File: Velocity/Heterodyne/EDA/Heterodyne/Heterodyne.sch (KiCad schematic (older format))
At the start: 40 parts, among them J1 OP_IN, J2 OP_OUT, J3 PWR, J4 Doppler_Out, J5 V_Square, J6 OP_OUT, J7 Reciever, J8 Emmiter, U1 SA612AD, U2 NE5532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

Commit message: changed up velocity heterodyne schematic to fix issues with wireing, and so provide a channel for sine wave driver amplification
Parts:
- removed C3, C4, C5: 100 nF, Capacitors_SMD:C_0805_HandSoldering, symbol Heterodyne-rescue:C-Device
- removed J1: OP_IN, Pin_Headers:Pin_Header_Straight_1x02_Pitch2.54mm, symbol Heterodyne-rescue:Conn_01x02-Connector_Generic
- removed J2: OP_OUT, Pin_Headers:Pin_Header_Straight_1x02_Pitch2.54mm, symbol Heterodyne-rescue:Conn_01x02-Connector_Generic
- removed R1, R3, R4, R5: 10 kΩ, Resistors_SMD:R_0805_HandSoldering, symbol Heterodyne-rescue:R-Device
- added R?: 39 kΩ, Resistors_SMD:R_0805_HandSoldering, symbol Heterodyne-rescue:R-Device
- added R? (x2): 1 kΩ, Resistors_SMD:R_0805_HandSoldering, symbol Heterodyne-rescue:R-Device
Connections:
- net GND: now also U2.4 (V-), R?.1; no longer U2.8 (V+)
- net VPP: now also U2.8 (V+), R?.1; no longer U2.4 (V-)
- net at J6.2 (Pin_2), U2.1: now also R?.2
- net at U2.2 (-): now also R?.1, R?.2, R?.2
- net Driver_Wave: now reaches U2.3 (+)
- net Driver_Wave: now also C10.2, C9.1, R10.2
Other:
- note added: "Consider Changing op amp to TL074"
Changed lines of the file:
@@
 L Heterodyne-rescue:NE5532-Amplifier_Operational U2
 U 3 1 5DE9ED64
-P 8250 3600
-F 0 "U2" H 8063 3555 50  0000 R CNN
-F 1 "NE5532" H 8063 3644 50  0000 R CNN
-F 2 "Housings_DIP:DIP-8_W7.62mm_LongPads" H 8250 3600 50  0001 C CNN
-F 3 "http://www.ti.com/lit/ds/symlink/ne5532.pdf" H 8250 3600 50  0001 C CNN
-	3    8250 3600
-	-1   0    0    1
-$EndComp
-$Comp
-L Heterodyne-rescue:VPP-power #PWR0111
-U 1 1 5DEA1CC4
-P 8350 3300
-F 0 "#PWR0111" H 8350 3150 50  0001 C CNN
-F 1 "VPP" V 8365 3426 50  0000 L CNN
-F 2 "" H 8350 3300 50  0001 C CNN
-F 3 "" H 8350 3300 50  0001 C CNN
-	1    8350 3300
-	1    0    0    -1
-$EndComp
-$Comp
-L Heterodyne-rescue:GND-power #PWR0112
-U 1 1 5DEA21FC
-P 8350 3900
-F 0 "#PWR0112" H 8350 3650 50  0001 C CNN
-F 1 "GND" V 8355 3773 50  0000 R CNN
-F 2 "" H 8350 3900 50  0001 C CNN
-F 3 "" H 8350 3900 50  0001 C CNN
-	1    8350 3900
+P 8450 3600
+F 0 "U2" H 8263 3555 50  0000 R CNN
+F 1 "NE5532" H 8263 3644 50  0000 R CNN
+F 2 "Housings_DIP:DIP-8_W7.62mm_LongPads" H 8450 3600 50  0001 C CNN
+F 3 "http://www.ti.com/lit/ds/symlink/ne5532.pdf" H 8450 3600 50  0001 C CNN
+	3    8450 3600
 	1    0    0    -1
 $EndComp
@@
 	0    -1   1    0
 $EndComp
-$Comp
-L Heterodyne-rescue:GND-power #PWR0117
-U 1 1 5DEC862E
-P 2450 2400
-F 0 "#PWR0117" H 2450 2150 50  0001 C CNN
-F 1 "GND" V 2455 2273 50  0000 R CNN
-F 2 "" H 2450 2400 50  0001 C CNN
-F 3 "" H 2450 2400 50  0001 C CNN
-	1    2450 2400
-	1    0    0    -1
-$EndComp
-$Comp
-L Heterodyne-rescue:GND-power #PWR0118
-U 1 1 5DEC895C
-P 1950 2400
-F 0 "#PWR0118" H 1950 2150 50  0001 C CNN
-F 1 "GND" V 1955 2273 50  0000 R CNN
-F 2 "" H 1950 2400 50  0001 C CNN
-F 3 "" H 1950 2400 50  0001 C CNN
-	1    1950 2400
-	1    0    0    -1
-$EndComp
-$Comp
-L Heterodyne-rescue:Conn_01x02-Connector_Generic J1
-U 1 1 5DECC74B
-P 2350 2200
-F 0 "J1" H 2430 2192 50  0000 L CNN
-F 1 "OP_IN" H 2430 2103 50  0000 L CNN
-F 2 "Pin_Headers:Pin_Header_Straight_1x02_Pitch2.54mm" H 2350 2200 50  0001 C CNN
-F 3 "~" H 2350 2200 50  0001 C CNN
-	1    2350 2200
-	0    -1   -1   0
-$EndComp
-$Comp
-L Heterodyne-rescue:Conn_01x02-Connector_Generic J2
-U 1 1 5DECCC45
-P 1950 2200
-F 0 "J2" H 2030 2192 50  0000 L CNN
-F 1 "OP_OUT" H 2030 2103 50  0000 L CNN
-F 2 "Pin_Headers:Pin_Header_Straight_1x02_Pitch2.54mm" H 1950 2200 50  0001 C CNN
-F 3 "~" H 1950 2200 50  0001 C CNN
-	1    1950 2200
-	0    -1   -1   0
-$EndComp
 Connection ~ 6150 4050
 Wire Wire Line
@@
 	5250 5100 5650 5100
 $Comp
-L Heterodyne-rescue:R-Device R4
-U 1 1 5DFAD002
-P 2350 2900
-F 0 "R4" V 2554 2900 50  0000 C CNN
-F 1 "10 kΩ" V 2465 2900 50  0000 C CNN
-F 2 "Resistors_SMD:R_0805_HandSoldering" V 2280 2900 50  0001 C CNN
-F 3 "~" H 2350 2900 50  0001 C CNN
-	1    2350 2900
-	1    0    0    -1
-$EndComp
-$Comp
-L Heterodyne-rescue:R-Device R3
-U 1 1 5DFAD398
-P 2050 2900
-F 0 "R3" V 2254 2900 50  0000 C CNN
-F 1 "10 kΩ" V 2165 2900 50  0000 C CNN
-F 2 "Resistors_SMD:R_0805_HandSoldering" V 1980 2900 50  0001 C CNN
-F 3 "~" H 2050 2900 50  0001 C CNN
-	1    2050 2900
-	1    0    0    -1
-$EndComp
-$Comp
-L Heterodyne-rescue:C-Device C4
-U 1 1 5DFADDA3
-P 2200 3250
-F 0 "C4" H 2085 3205 50  0000 R CNN
-F 1 "100 nF" H 2085 3294 50  0000 R CNN
-F 2 "Capacitors_SMD:C_0805_HandSoldering" H 2238 3100 50  0001 C CNN
-F 3 "~" H 2200 3250 50  0001 C CNN
-	1    2200 3250
-	0    -1   -1   0
-$EndComp
-$Comp
-L Heterodyne-rescue:R-Device R5
-U 1 1 5DFAEA80
-P 2600 3850
-F 0 "R5" V 2804 3850 50  0000 C CNN
-F 1 "10 kΩ" V 2715 3850 50  0000 C CNN
-F 2 "Resistors_SMD:R_0805_HandSoldering" V 2530 3850 50  0001 C CNN
-F 3 "~" H 2600 3850 50  0001 C CNN
-	1    2600 3850
-	1    0    0    -1
-$EndComp
-$Comp
-L Heterodyne-rescue:R-Device R1
-U 1 1 5DFAEDEA
-P 1450 3850
-F 0 "R1" V 1654 3850 50  0000 C CNN
-F 1 "10 kΩ" V 1565 3850 50  0000 C CNN
-F 2 "Resistors_SMD:R_0805_HandSoldering" V 1380 3850 50  0001 C CNN
-F 3 "~" H 1450 3850 50  0001 C CNN
-	1    1450 3850
-	1    0    0    -1
-$EndComp
-$Comp
-L Heterodyne-rescue:C-Device C5
-U 1 1 5DFAF0E1
-P 2950 3850
-F 0 "C5" V 3199 3850 50  0000 C CNN
-F 1 "100 nF" V 3110 3850 50  0000 C CNN
-F 2 "Capacitors_SMD:C_0805_HandSoldering" H 2988 3700 50  0001 C CNN
-F 3 "~" H 2950 3850 50  0001 C CNN
-	1    2950 3850
-	1    0    0    -1
-$EndComp
-$Comp
-L Heterodyne-rescue:C-Device C3
-U 1 1 5DFB2EFF
-P 1100 3850
-F 0 "C3" V 1349 3850 50  0000 C CNN
-F 1 "100 nF" V 1260 3850 50  0000 C CNN
-F 2 "Capacitors_SMD:C_0805_HandSoldering" H 1138 3700 50  0001 C CNN
-F 3 "~" H 1100 3850 50  0001 C CNN
-	1    1100 3850
-	1    0    0    -1
-$EndComp
-$Comp
 L Heterodyne-rescue:GND-power #PWR0120
 U 1 1 5DFB3A2A
@@
 $EndComp
 Wire Wire Line
-	2150 4150 2600 4150
-Wire Wire Line
-	2600 4150 2600 4000
-Wire Wire Line
-	2350 3050 2350 3250
-Wire Wire Line
-	2350 3250 2350 3550
-Wire Wire Line
 	2250 3550 2350 3550
-Connection ~ 2350 3250
 Connection ~ 2350 3550
-Wire Wire Line
-	2350 3550 2600 3550
-Wire Wire Line
-	2050 3550 2050 3250
-Wire Wire Line
-	2050 3250 2050 3050
-Connection ~ 2050 3250
-Wire Wire Line
-	2350 2400 2350 2750
-Wire Wire Line
-	2050 2400 2050 2750
-Wire Wire Line
-	2950 4000 2950 4150
-Wire Wire Line
-	2950 4150 2600 4150
-Connection ~ 2600 4150
-Wire Wire Line
-	2950 3700 2950 3550
-Wire Wire Line
-	2950 3550 2600 3550
-Connection ~ 2600 3550
-Wire Wire Line
-	2050 3250 1450 3250
-Wire Wire Line
-	1450 3250 1450 3700
-Wire Wire Line
-	1450 3250 1100 3250
-Wire Wire Line
-	1100 3250 1100 3700
-Wire Wire Line
-	2600 3550 2600 3700
-Connection ~ 1450 3250
-Wire Wire Line
-	1100 4000 1450 4000
-Wire Wire Line
-	2150 4150 1450 4150
-Wire Wire Line
-	1450 4150 1450 4000
-Connection ~ 2150 4150
-Connection ~ 1450 4000
 Wire Wire Line
 	2150 4150 2150 4350
@@
 $EndComp
 Wire Wire Line
-	8350 3300 8050 3300
-Wire Wire Line
 	8050 3300 8050 3450
-Connection ~ 8350 3300
 Wire Wire Line
 	8050 3750 8050 3900
-Wire Wire Line
-	8050 3900 8350 3900
-Connection ~ 8350 3900
 Connection ~ 6900 1850
 Connection ~ 6900 1550
+Wire Wire Line
+	8050 3300 8350 3300
+Wire Wire Line
+	8050 3900 8350 3900
+$Comp
+L Heterodyne-rescue:VPP-power #PWR?
+U 1 1 5E281BA1
+P 8350 3300
+F 0 "#PWR?" H 8350 3150 50  0001 C CNN
+F 1 "VPP" H 8365 3471 50  0000 C CNN
+F 2 "" H 8350 3300 50  0001 C CNN
+F 3 "" H 8350 3300 50  0001 C CNN
+	1    8350 3300
+	1    0    0    -1
+$EndComp
+Connection ~ 8350 3300
+$Comp
+L Heterodyne-rescue:GND-power #PWR?
+U 1 1 5E282178
+P 8350 3900
+F 0 "#PWR?" H 8350 3650 50  0001 C CNN
+F 1 "GND" H 8355 3729 50  0000 C CNN
+F 2 "" H 8350 3900 50  0001 C CNN
+F 3 "" H 8350 3900 50  0001 C CNN
+	1    8350 3900
+	1    0    0    -1
+$EndComp
+Connection ~ 8350 3900
+Wire Wire Line
+	2050 3050 2050 3550
+$Comp
+L Heterodyne-rescue:R-Device R?
+U 1 1 5E282544
+P 2650 3850
+F 0 "R?" V 2854 3850 50  0000 C CNN
+F 1 "39 kΩ" V 2765 3850 50  0000 C CNN
+F 2 "Resistors_SMD:R_0805_HandSoldering" V 2580 3850 50  0001 C CNN
+F 3 "~" H 2650 3850 50  0001 C CNN
+	1    2650 3850
+	1    0    0    -1
+$EndComp
+Wire Wire Line
+	2150 4150 2650 4150
+Wire Wire Line
+	2650 4150 2650 4000
+Connection ~ 2150 4150
+Wire Wire Line
+	2650 3700 2650 3550
+Wire Wire Line
+	2350 3550 2650 3550
+$Comp
+L Heterodyne-rescue:R-Device R?
+U 1 1 5E285F20
+P 2350 2800
+F 0 "R?" V 2554 2800 50  0000 C CNN
+F 1 "1 kΩ" V 2465 2800 50  0000 C CNN
+F 2 "Resistors_SMD:R_0805_HandSoldering" V 2280 2800 50  0001 C CNN
+F 3 "~" H 2350 2800 50  0001 C CNN
+	1    2350 2800
+	1    0    0    -1
+$EndComp
+$Comp
+L Heterodyne-rescue:R-Device R?
+U 1 1 5E286294
+P 2600 3050
+F 0 "R?" V 2804 3050 50  0000 C CNN
+F 1 "1 kΩ" V 2715 3050 50  0000 C CNN
+F 2 "Resistors_SMD:R_0805_HandSoldering" V 2530 3050 50  0001 C CNN
+F 3 "~" H 2600 3050 50  0001 C CNN
+	1    2600 3050
+	0    1    1    0
+$EndComp
+Wire Wire Line
+	2350 2950 2350 3050
+Wire Wire Line
+	2450 3050 2350 3050
+Connection ~ 2350 3050
+Wire Wire Line
+	2350 3050 2350 3550
+$Comp
+L Heterodyne-rescue:VPP-power #PWR?
+U 1 1 5E289D11
+P 2350 2650
+F 0 "#PWR?" H 2350 2500 50  0001 C CNN
+F 1 "VPP" H 2365 2821 50  0000 C CNN
+F 2 "" H 2350 2650 50  0001 C CNN
+F 3 "" H 2350 2650 50  0001 C CNN
+	1    2350 2650
+	1    0    0    -1
+$EndComp
+$Comp
+L Heterodyne-rescue:GND-power #PWR?
+U 1 1 5E28A11D
+P 2750 3050
+F 0 "#PWR?" H 2750 2800 50  0001 C CNN
+F 1 "GND" H 2755 2879 50  0000 C CNN
+F 2 "" H 2750 3050 50  0001 C CNN
+F 3 "" H 2750 3050 50  0001 C CNN
+	1    2750 3050
+	0    -1   -1   0
+$EndComp
+Text GLabel 6700 2550 1    50   Input ~ 0
+Driver_Wave
+Text GLabel 2050 3050 1    50   Input ~ 0
+Driver_Wave
+Text Notes 1000 800  0    50   ~ 0
+Consider Changing op amp to TL074
 $EndSCHEMATC

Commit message: daily commit
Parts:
- gave numbers to parts that had none: 3
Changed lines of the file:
@@
 	8050 3900 8350 3900
 $Comp
-L Heterodyne-rescue:VPP-power #PWR?
+L Heterodyne-rescue:VPP-power #PWR0111
 U 1 1 5E281BA1
 P 8350 3300
-F 0 "#PWR?" H 8350 3150 50  0001 C CNN
+F 0 "#PWR0111" H 8350 3150 50  0001 C CNN
 F 1 "VPP" H 8365 3471 50  0000 C CNN
 F 2 "" H 8350 3300 50  0001 C CNN
@@
 Connection ~ 8350 3300
 $Comp
-L Heterodyne-rescue:GND-power #PWR?
+L Heterodyne-rescue:GND-power #PWR0112
 U 1 1 5E282178
 P 8350 3900
-F 0 "#PWR?" H 8350 3650 50  0001 C CNN
+F 0 "#PWR0112" H 8350 3650 50  0001 C CNN
 F 1 "GND" H 8355 3729 50  0000 C CNN
 F 2 "" H 8350 3900 50  0001 C CNN
@@
 	2050 3050 2050 3550
 $Comp
-L Heterodyne-rescue:R-Device R?
+L Heterodyne-rescue:R-Device R4
 U 1 1 5E282544
 P 2650 3850
-F 0 "R?" V 2854 3850 50  0000 C CNN
+F 0 "R4" V 2854 3850 50  0000 C CNN
 F 1 "39 kΩ" V 2765 3850 50  0000 C CNN
 F 2 "Resistors_SMD:R_0805_HandSoldering" V 2580 3850 50  0001 C CNN
@@
 	2350 3550 2650 3550
 $Comp
-L Heterodyne-rescue:R-Device R?
+L Heterodyne-rescue:R-Device R1
 U 1 1 5E285F20
 P 2350 2800
-F 0 "R?" V 2554 2800 50  0000 C CNN
+F 0 "R1" V 2554 2800 50  0000 C CNN
 F 1 "1 kΩ" V 2465 2800 50  0000 C CNN
 F 2 "Resistors_SMD:R_0805_HandSoldering" V 2280 2800 50  0001 C CNN
@@
 $EndComp
 $Comp
-L Heterodyne-rescue:R-Device R?
+L Heterodyne-rescue:R-Device R3
 U 1 1 5E286294
 P 2600 3050
-F 0 "R?" V 2804 3050 50  0000 C CNN
+F 0 "R3" V 2804 3050 50  0000 C CNN
 F 1 "1 kΩ" V 2715 3050 50  0000 C CNN
 F 2 "Resistors_SMD:R_0805_HandSoldering" V 2530 3050 50  0001 C CNN
@@
 	2350 3050 2350 3550
 $Comp
-L Heterodyne-rescue:VPP-power #PWR?
+L Heterodyne-rescue:VPP-power #PWR0117
 U 1 1 5E289D11
 P 2350 2650
-F 0 "#PWR?" H 2350 2500 50  0001 C CNN
+F 0 "#PWR0117" H 2350 2500 50  0001 C CNN
 F 1 "VPP" H 2365 2821 50  0000 C CNN
 F 2 "" H 2350 2650 50  0001 C CNN
@@
 $EndComp
 $Comp
-L Heterodyne-rescue:GND-power #PWR?
+L Heterodyne-rescue:GND-power #PWR0118
 U 1 1 5E28A11D
 P 2750 3050
-F 0 "#PWR?" H 2750 2800 50  0001 C CNN
+F 0 "#PWR0118" H 2750 2800 50  0001 C CNN
 F 1 "GND" H 2755 2879 50  0000 C CNN
 F 2 "" H 2750 3050 50  0001 C CNN

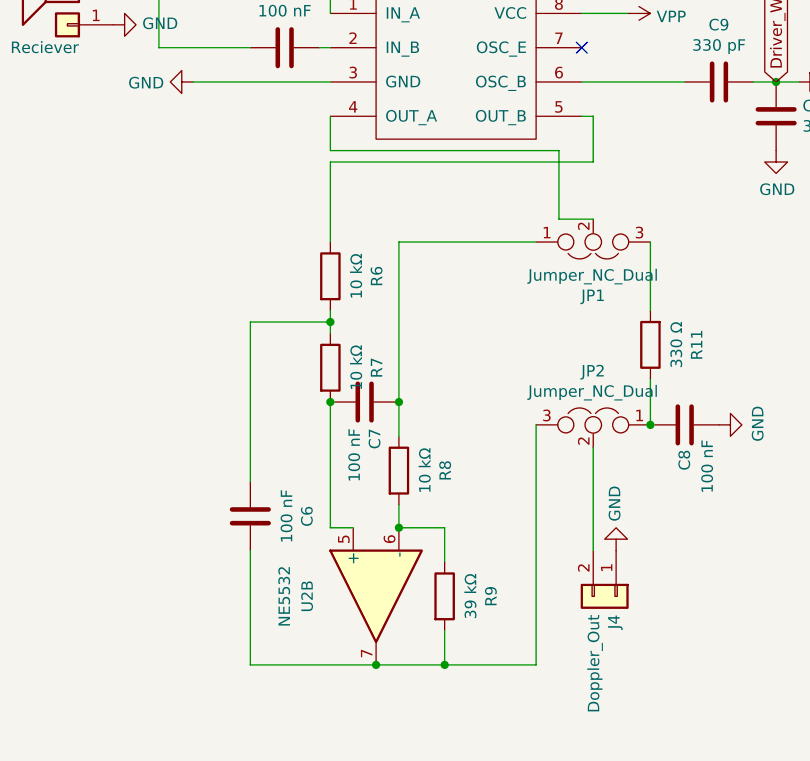
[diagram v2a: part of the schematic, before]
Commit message: added updates to heterodyne code to take averages of multiple FFTs changed up heterodyne circuit to fix bugs
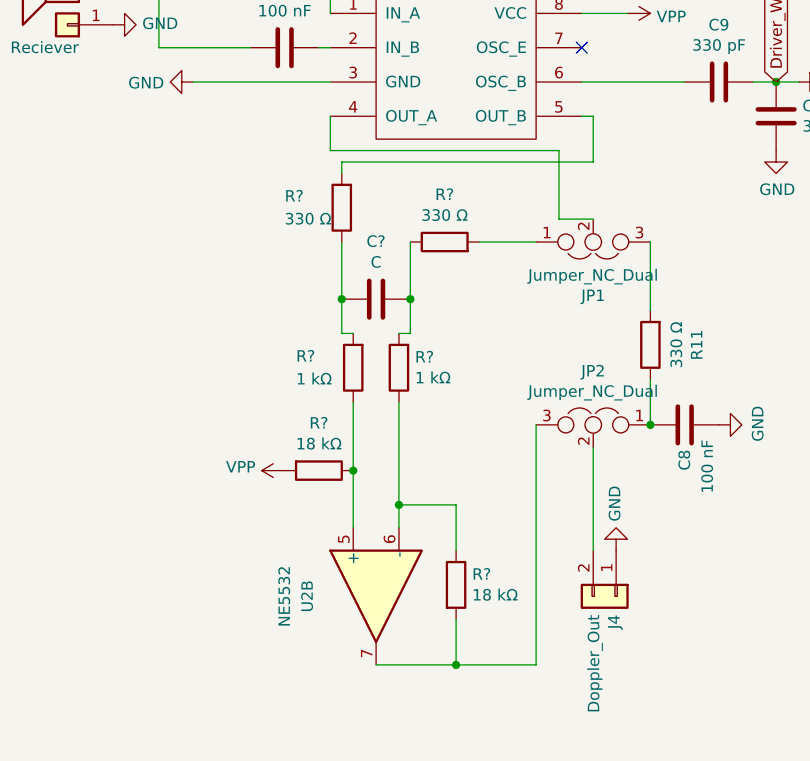
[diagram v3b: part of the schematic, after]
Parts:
- removed C6, C7: 100 nF, Capacitors_SMD:C_0805_HandSoldering, symbol Heterodyne-rescue:C-Device
- removed R6, R7, R8: 10 kΩ, Resistors_SMD:R_0805_HandSoldering, symbol Heterodyne-rescue:R-Device
- removed R9: 39 kΩ, Resistors_SMD:R_0805_HandSoldering, symbol Heterodyne-rescue:R-Device
- added C?: C, symbol Device:C
- added R? (x2): 18 kΩ, symbol Device:R
- added R? (x2): 1 kΩ, symbol Device:R
- added R? (x2): 330 Ω, symbol Device:R
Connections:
- net VPP: now also R?.2
- net at U1.5 (OUT_B): now also R?.2
- net at U2.5 (+): now also R?.1, R?.1
- net at U2.6 (-): now also R?.1, R?.1
- net at JP2.3, U2.7: now also R?.2
- net at JP1.1: now also R?.2
- new net: C?.2, R?.1, R?.2
- new net: C?.1, R?.1, R?.2
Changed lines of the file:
@@
-$EndComp
-$Comp
-L Heterodyne-rescue:R-Device R8
-U 1 1 5DF78A40
-P 5050 4250
-F 0 "R8" V 5254 4250 50  0000 C CNN
-F 1 "10 kΩ" V 5165 4250 50  0000 C CNN
-F 2 "Resistors_SMD:R_0805_HandSoldering" V 4980 4250 50  0001 C CNN
-F 3 "~" H 5050 4250 50  0001 C CNN
-	1    5050 4250
-	1    0    0    -1
-$EndComp
-$Comp
-L Heterodyne-rescue:R-Device R9
-U 1 1 5DF72BBA
-P 5250 4800
-F 0 "R9" V 5454 4800 50  0000 C CNN
-F 1 "39 kΩ" V 5365 4800 50  0000 C CNN
-F 2 "Resistors_SMD:R_0805_HandSoldering" V 5180 4800 50  0001 C CNN
-F 3 "~" H 5250 4800 50  0001 C CNN
-	1    5250 4800
-	1    0    0    -1
 $EndComp
 $Comp
@@
 $EndComp
 Wire Wire Line
-	4950 5100 5250 5100
-Wire Wire Line
-	5250 5100 5250 4950
-Wire Wire Line
-	5250 4650 5250 4500
-Wire Wire Line
-	5250 4500 5050 4500
-Wire Wire Line
-	5050 4500 5050 4400
-Connection ~ 5050 4500
-$Comp
-L Heterodyne-rescue:C-Device C7
-U 1 1 5DF80B53
-P 4900 3950
-F 0 "C7" H 4785 3905 50  0000 R CNN
-F 1 "100 nF" H 4785 3994 50  0000 R CNN
-F 2 "Capacitors_SMD:C_0805_HandSoldering" H 4938 3800 50  0001 C CNN
-F 3 "~" H 4900 3950 50  0001 C CNN
-	1    4900 3950
-	0    -1   -1   0
-$EndComp
-Wire Wire Line
-	4850 4500 4750 4500
-Wire Wire Line
-	4750 4500 4750 3950
-Wire Wire Line
-	5050 3950 5050 4100
-$Comp
-L Heterodyne-rescue:R-Device R7
-U 1 1 5DF84FFF
-P 4750 3800
-F 0 "R7" V 4954 3800 50  0000 C CNN
-F 1 "10 kΩ" V 4865 3800 50  0000 C CNN
-F 2 "Resistors_SMD:R_0805_HandSoldering" V 4680 3800 50  0001 C CNN
-F 3 "~" H 4750 3800 50  0001 C CNN
-	1    4750 3800
-	1    0    0    -1
-$EndComp
-Connection ~ 4750 3950
-$Comp
-L Heterodyne-rescue:R-Device R6
-U 1 1 5DF8534D
-P 4750 3400
-F 0 "R6" V 4954 3400 50  0000 C CNN
-F 1 "10 kΩ" V 4865 3400 50  0000 C CNN
-F 2 "Resistors_SMD:R_0805_HandSoldering" V 4680 3400 50  0001 C CNN
-F 3 "~" H 4750 3400 50  0001 C CNN
-	1    4750 3400
-	1    0    0    -1
-$EndComp
-$Comp
-L Heterodyne-rescue:C-Device C6
-U 1 1 5DF85649
-P 4400 4450
-F 0 "C6" V 4649 4450 50  0000 C CNN
-F 1 "100 nF" V 4560 4450 50  0000 C CNN
-F 2 "Capacitors_SMD:C_0805_HandSoldering" H 4438 4300 50  0001 C CNN
-F 3 "~" H 4400 4450 50  0001 C CNN
-	1    4400 4450
-	1    0    0    -1
-$EndComp
-Wire Wire Line
-	4400 4600 4400 5100
-Wire Wire Line
-	4400 5100 4950 5100
-Connection ~ 4950 5100
-Wire Wire Line
-	4400 4300 4400 3600
-Wire Wire Line
-	4400 3600 4750 3600
-Wire Wire Line
-	4750 3600 4750 3650
-Wire Wire Line
-	4750 3550 4750 3600
-Connection ~ 4750 3600
-Wire Wire Line
-	5050 3950 5050 3250
-Connection ~ 5050 3950
-Wire Wire Line
-	5650 3250 5050 3250
-Wire Wire Line
 	5650 5100 5650 4050
-Connection ~ 5250 5100
-Wire Wire Line
-	5250 5100 5650 5100
 $Comp
 L Heterodyne-rescue:GND-power #PWR0120
@@
 	5900 2700 5900 2900
 Wire Wire Line
-	5900 2900 4750 2900
-Wire Wire Line
-	4750 2900 4750 3250
-Wire Wire Line
 	4750 2850 5750 2850
 Wire Wire Line
@@
 Text Notes 1000 800  0    50   ~ 0
 Consider Changing op amp to TL074
+Wire Wire Line
+	4950 5100 5300 5100
+$Comp
+L Device:R R?
+U 1 1 5E37EFD3
+P 5300 4750
+F 0 "R?" H 5370 4796 50  0000 L CNN
+F 1 "18 kΩ" H 5370 4705 50  0000 L CNN
+F 2 "" V 5230 4750 50  0001 C CNN
+F 3 "~" H 5300 4750 50  0001 C CNN
+	1    5300 4750
+	1    0    0    -1
+$EndComp
+Wire Wire Line
+	5300 4900 5300 5100
+Connection ~ 5300 5100
+Wire Wire Line
+	5300 5100 5650 5100
+Wire Wire Line
+	5300 4600 5300 4400
+Wire Wire Line
+	5300 4400 5050 4400
+Wire Wire Line
+	5050 4400 5050 4500
+$Comp
+L Device:R R?
+U 1 1 5E3820B6
+P 4700 4250
+F 0 "R?" V 4493 4250 50  0000 C CNN
+F 1 "18 kΩ" V 4584 4250 50  0000 C CNN
+F 2 "" V 4630 4250 50  0001 C CNN
+F 3 "~" H 4700 4250 50  0001 C CNN
+	1    4700 4250
+	0    1    1    0
+$EndComp
+$Comp
+L Heterodyne-rescue:VPP-power #PWR?
+U 1 1 5E3824B9
+P 4550 4250
+F 0 "#PWR?" H 4550 4100 50  0001 C CNN
+F 1 "VPP" V 4565 4377 50  0000 L CNN
+F 2 "" H 4550 4250 50  0001 C CNN
+F 3 "" H 4550 4250 50  0001 C CNN
+	1    4550 4250
+	0    -1   -1   0
+$EndComp
+$Comp
+L Device:R R?
+U 1 1 5E382D5B
+P 4850 3800
+F 0 "R?" H 5100 3750 50  0000 R CNN
+F 1 "1 kΩ" H 5100 3850 50  0000 R CNN
+F 2 "" V 4780 3800 50  0001 C CNN
+F 3 "~" H 4850 3800 50  0001 C CNN
+	1    4850 3800
+	-1   0    0    1
+$EndComp
+$Comp
+L Device:R R?
+U 1 1 5E383109
+P 5050 3800
+F 0 "R?" H 4980 3754 50  0000 R CNN
+F 1 "1 kΩ" H 4980 3845 50  0000 R CNN
+F 2 "" V 4980 3800 50  0001 C CNN
+F 3 "~" H 5050 3800 50  0001 C CNN
+	1    5050 3800
+	-1   0    0    1
+$EndComp
+Wire Wire Line
+	5050 3950 5050 4400
+Connection ~ 5050 4400
+Wire Wire Line
+	4850 4500 4850 4250
+Wire Wire Line
+	4850 3950 4850 4250
+Connection ~ 4850 4250
+$Comp
+L Device:C C?
+U 1 1 5E387E65
+P 4950 3500
+F 0 "C?" V 4698 3500 50  0000 C CNN
+F 1 "C" V 4789 3500 50  0000 C CNN
+F 2 "" H 4988 3350 50  0001 C CNN
+F 3 "~" H 4950 3500 50  0001 C CNN
+	1    4950 3500
+	0    1    1    0
+$EndComp
+Wire Wire Line
+	5050 3650 5100 3650
+Wire Wire Line
+	5100 3650 5100 3500
+Wire Wire Line
+	4850 3650 4800 3650
+Wire Wire Line
+	4800 3650 4800 3500
+$Comp
+L Device:R R?
+U 1 1 5E38B726
+P 5250 3250
+F 0 "R?" V 5457 3250 50  0000 C CNN
+F 1 "330 Ω" V 5366 3250 50  0000 C CNN
+F 2 "" V 5180 3250 50  0001 C CNN
+F 3 "~" H 5250 3250 50  0001 C CNN
+	1    5250 3250
+	0    -1   -1   0
+$EndComp
+$Comp
+L Device:R R?
+U 1 1 5E38C4E7
+P 4800 3100
+F 0 "R?" H 5050 3050 50  0000 R CNN
+F 1 "330 Ω" H 5050 3150 50  0000 R CNN
+F 2 "" V 4730 3100 50  0001 C CNN
+F 3 "~" H 4800 3100 50  0001 C CNN
+	1    4800 3100
+	-1   0    0    1
+$EndComp
+Wire Wire Line
+	4800 2900 4800 2950
+Wire Wire Line
+	4800 2900 5900 2900
+Wire Wire Line
+	4800 3250 4800 3500
+Connection ~ 4800 3500
+Wire Wire Line
+	5100 3500 5100 3250
+Connection ~ 5100 3500
+Wire Wire Line
+	5400 3250 5650 3250
 $EndSCHEMATC
